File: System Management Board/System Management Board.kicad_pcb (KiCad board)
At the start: 4 copper layers, 150 x 110 mm, 72 parts, among them IC1 SI2318CDS-T1-GE3, IC2 SI2318CDS-T1-GE3, IC3 SI2318CDS-T1-GE3, IC4 SI2318CDS-T1-GE3, IC5 SI2318CDS-T1-GE3, J1 Conn_01x04_Male, J10 Conn_01x02_Male, J11 Conn_02x20_Odd_Even, J2 Conn_01x04_Male, J3 Conn_01x02_Male, J4 PJ-063BH, J5 Conn_01x02_Male, J6 Conn_02x06_Counter_Clockwise, J7 Conn_02x20_Odd_Even, J8 Conn_01x02_Male, J9 Conn_01x02_Male, K1 J115F11CH5VDCS61.5U, K2 J114FL1CS165VDC.41, K3 J114FL1CS165VDC.41, U1 SC0915, U2 OKI-78SR-5/1.5-W36E-C, U3 OKI-78SR-5/1.5-W36E-C, U4 AP7375-50W5-7

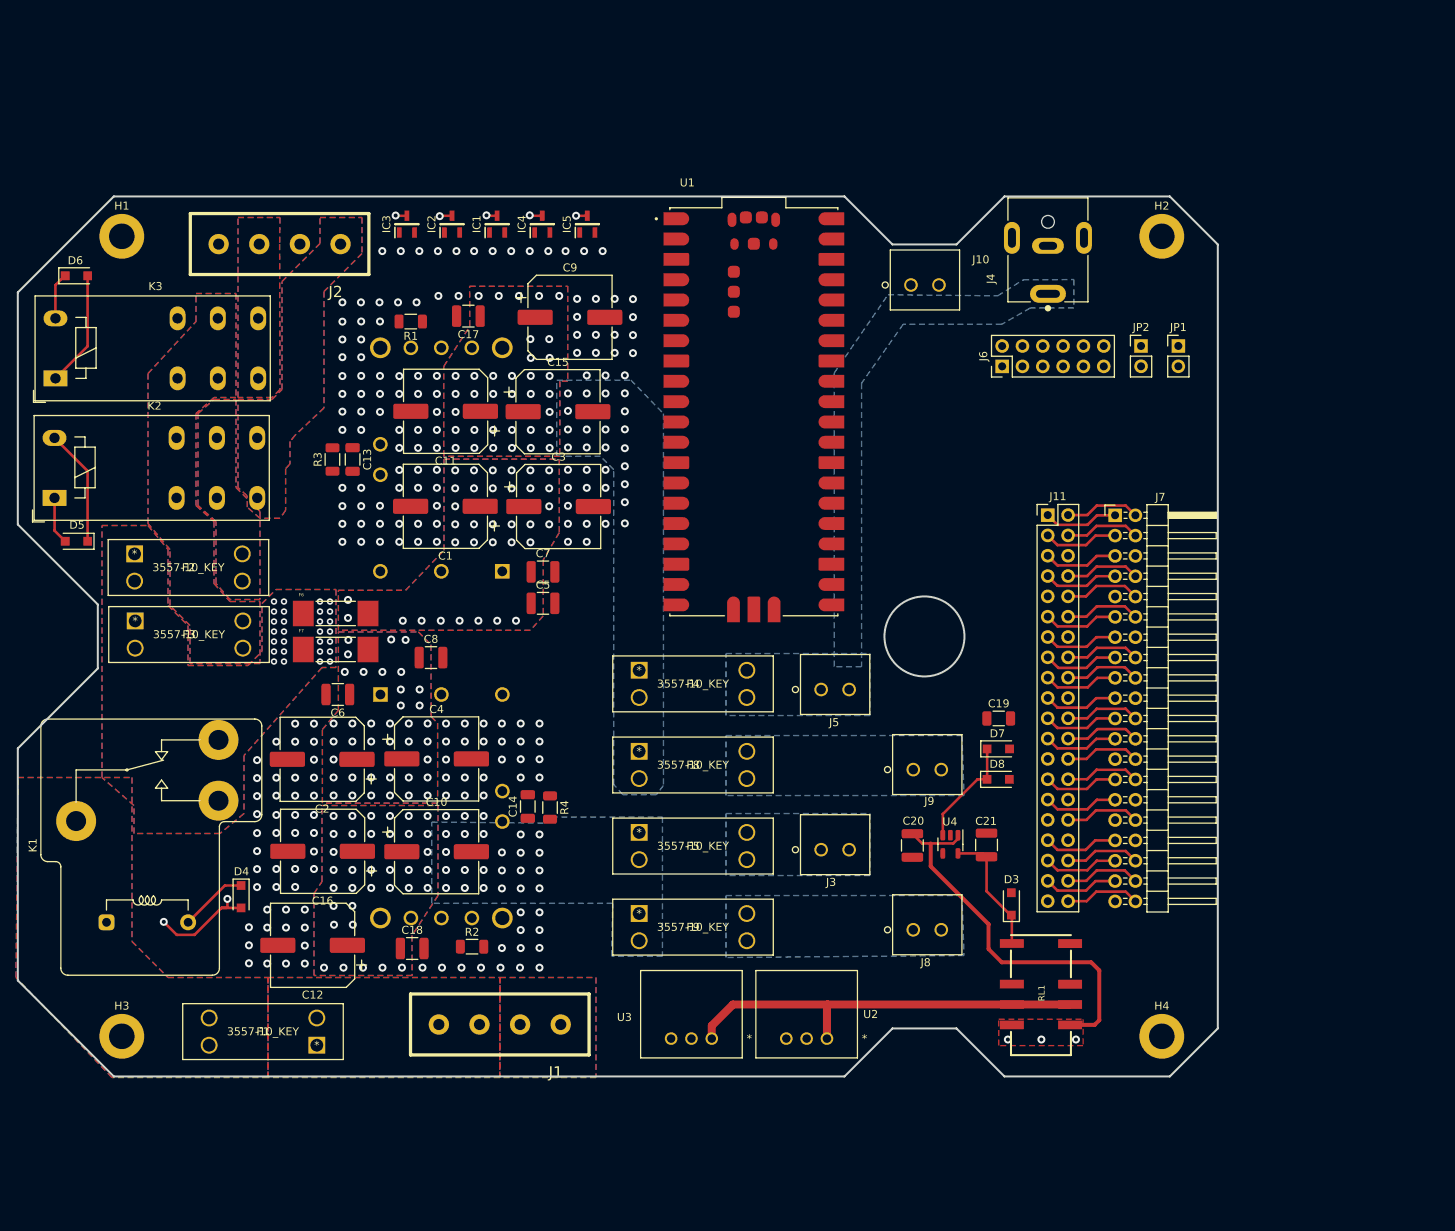
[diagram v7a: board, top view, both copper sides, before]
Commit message: Added analog mux ckt and placed componets
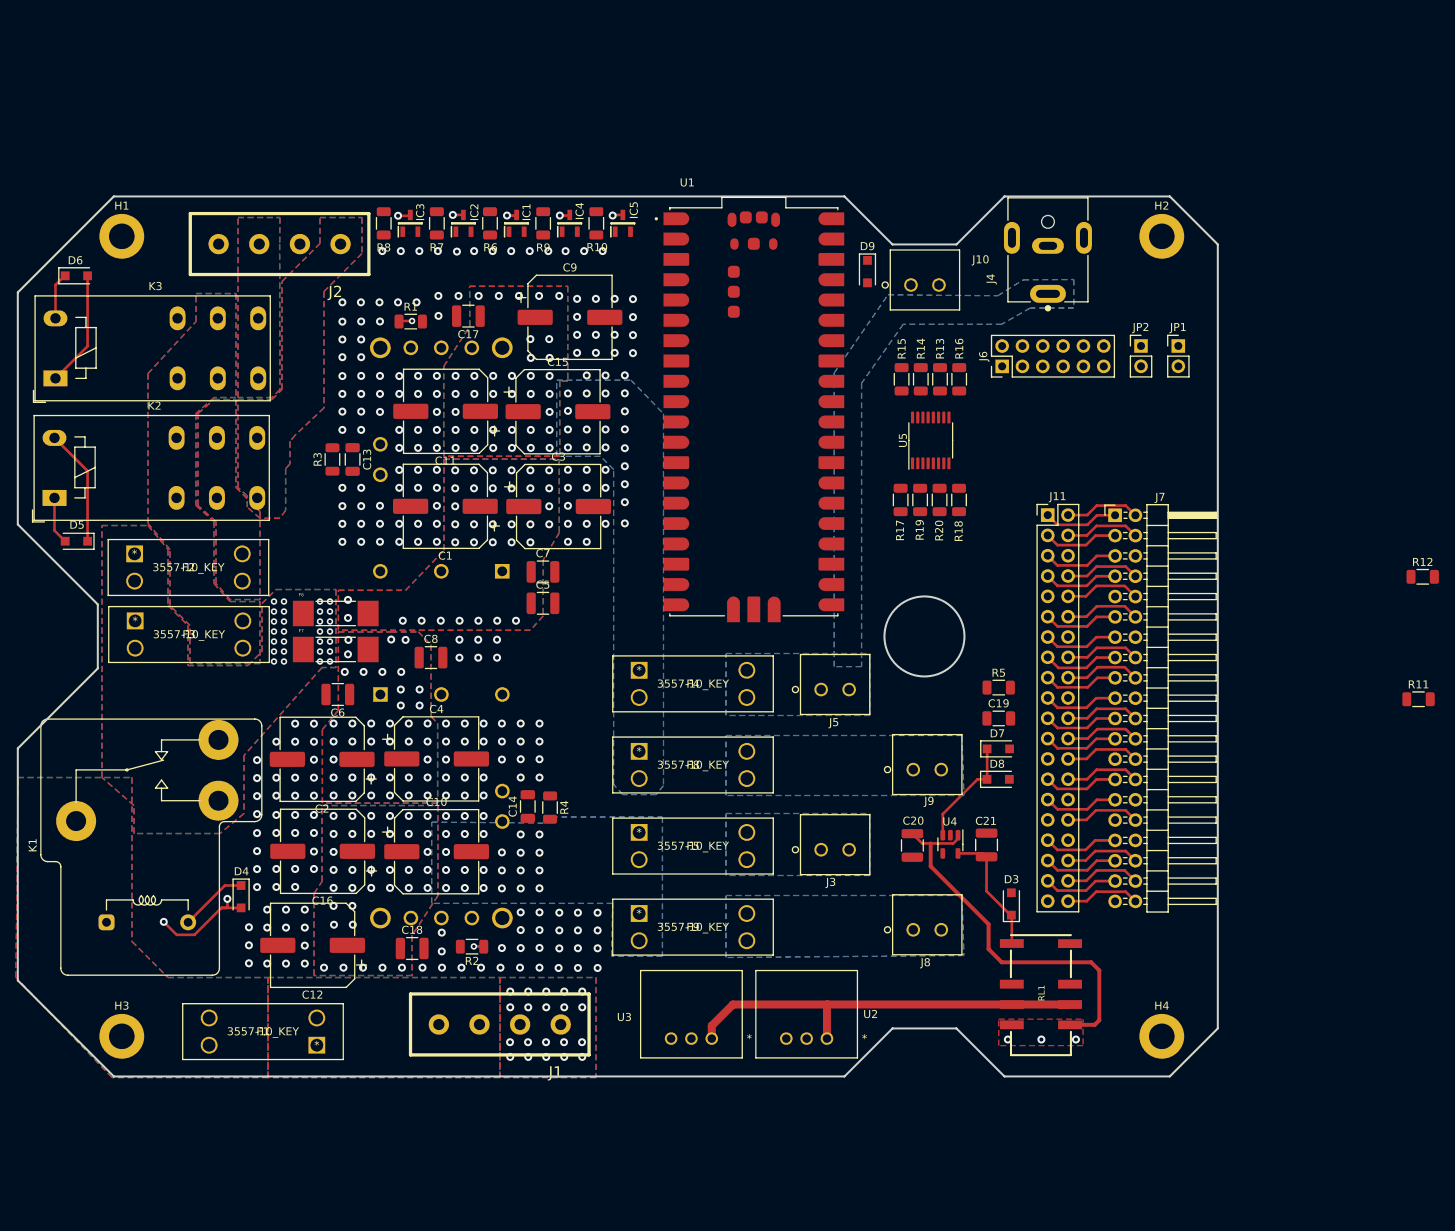
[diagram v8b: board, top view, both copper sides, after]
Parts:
- added D9: D, Diode_SMD:D_SOD-123F, F.Cu at (179.9, 54.8)
- added R10: 10k, Resistor_SMD:R_1206_3216Metric, F.Cu at (146.0, 48.7)
- added R11: 10k, Resistor_SMD:R_1206_3216Metric, F.Cu at (248.8, 108.2)
- added R12: 100k, Resistor_SMD:R_1206_3216Metric, F.Cu at (249.3, 92.9)
- added R13: 10k, Resistor_SMD:R_1206_3216Metric, F.Cu at (189.0, 68.2)
- added R14: 10k, Resistor_SMD:R_1206_3216Metric, F.Cu at (186.6, 68.2)
- added R15: 10k, Resistor_SMD:R_1206_3216Metric, F.Cu at (184.2, 68.2)
- added R16: 10k, Resistor_SMD:R_1206_3216Metric, F.Cu at (191.4, 68.2)
- added R17: 10k, Resistor_SMD:R_1206_3216Metric, F.Cu at (184.1, 83.3)
- added R18: 10k, Resistor_SMD:R_1206_3216Metric, F.Cu at (191.4, 83.3)
- added R19: 10k, Resistor_SMD:R_1206_3216Metric, F.Cu at (186.5, 83.3)
- added R20: 10k, Resistor_SMD:R_1206_3216Metric, F.Cu at (188.9, 83.3)
- added R5: 10k, Resistor_SMD:R_1206_3216Metric, F.Cu at (196.3, 106.8)
- added R6: 10k, Resistor_SMD:R_1206_3216Metric, F.Cu at (132.8, 48.7)
- added R7: 10k, Resistor_SMD:R_1206_3216Metric, F.Cu at (126.1, 48.7)
- added R8: 10k, Resistor_SMD:R_1206_3216Metric, F.Cu at (119.5, 48.7)
- added R9: 10k, Resistor_SMD:R_1206_3216Metric, F.Cu at (139.4, 48.7)
- added U5: 74HC4051, Package_SO:TSSOP-16_4.4x5mm_P0.65mm, F.Cu at (187.8, 75.9)
- moved IC5 4.45 mm to (149.4, 48.7)
- moved IC4 3.44 mm to (142.7, 48.7)
- moved IC1 2.44 mm to (136.1, 48.7)
- moved IC2 1.43 mm to (129.4, 48.7)
- moved IC3 0.43 mm to (122.8, 48.7)
- turned R1 to 0 degrees
- turned R2 to 180 degrees
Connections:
- C13 pad 1: Net-(C13-Pad1) -> /COMP PWR CM
- C14 pad 1: Net-(C14-Pad1) -> /POE SW PWR CM
- PS1 pad 34: Net-(C13-Pad1) -> /COMP PWR CM
- PS2 pad 34: Net-(C14-Pad1) -> /POE SW PWR CM
- R3 pad 2: Net-(C13-Pad1) -> /COMP PWR CM
- R4 pad 2: Net-(C14-Pad1) -> /POE SW PWR CM
- U1 pad 11: unconnected-(U1-Pad11) -> Net-(U1-Pad11)
- U1 pad 12: unconnected-(U1-Pad12) -> Net-(U1-Pad12)
- U1 pad 17: unconnected-(U1-Pad17) -> Net-(U1-Pad17)
- U1 pad 19: unconnected-(U1-Pad19) -> /COMP PWR GOOD
- U1 pad 20: unconnected-(U1-Pad20) -> /SWITCH PWR GOOD
- U1 pad 26: unconnected-(U1-Pad26) -> /MUX_S0
- U1 pad 27: unconnected-(U1-Pad27) -> /MUX_S1
- U1 pad 29: unconnected-(U1-Pad29) -> /MUX_S2
- U1 pad 31: /Vin_MES_ADC -> /Analog Mux OUT
- U1 pad 32: unconnected-(U1-Pad32) -> /COMP PWR CM
- U1 pad 34: unconnected-(U1-Pad34) -> /POE SW PWR CM
- U1 pad 36: unconnected-(U1-Pad36) -> /PICO 3V3
- U1 pad 39: /5V Logic PWR -> Net-(U1-Pad39)
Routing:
- net /~{COMP PWR EN}: track 55.4 -> 67.1 mm
- net Net-(PS1-Pad6): track 0.00 -> 6.80 mm, vias 0 -> 1
- net Net-(PS2-Pad6): track 0.00 -> 6.78 mm, vias 0 -> 1
- net Net-(K1-PadA1): track 137.4 -> 139.8 mm
- net Net-(K2-PadA1): track 80.0 -> 80.9 mm
- net /~{SWITCH PWR EN}: track 76.7 -> 77.5 mm
- net GND: vias 229 -> 270
